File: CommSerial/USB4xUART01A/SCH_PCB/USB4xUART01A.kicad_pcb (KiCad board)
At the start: 2 copper layers, 40.1 x 40.1 mm, 31 parts, among them J1 HEADER_2x04_PARALLEL, J2 HEADER_2x04_PARALLEL, J3 HEADER_1x02, J4 HEADER_1x02, J5 HEADER_1x02, J6 HEADER_1x02, J7 HEADER_2x04_PARALLEL, J8 HEADER_2x04_PARALLEL, M1 HOLE, M2 HOLE, M3 HOLE, M4 HOLE

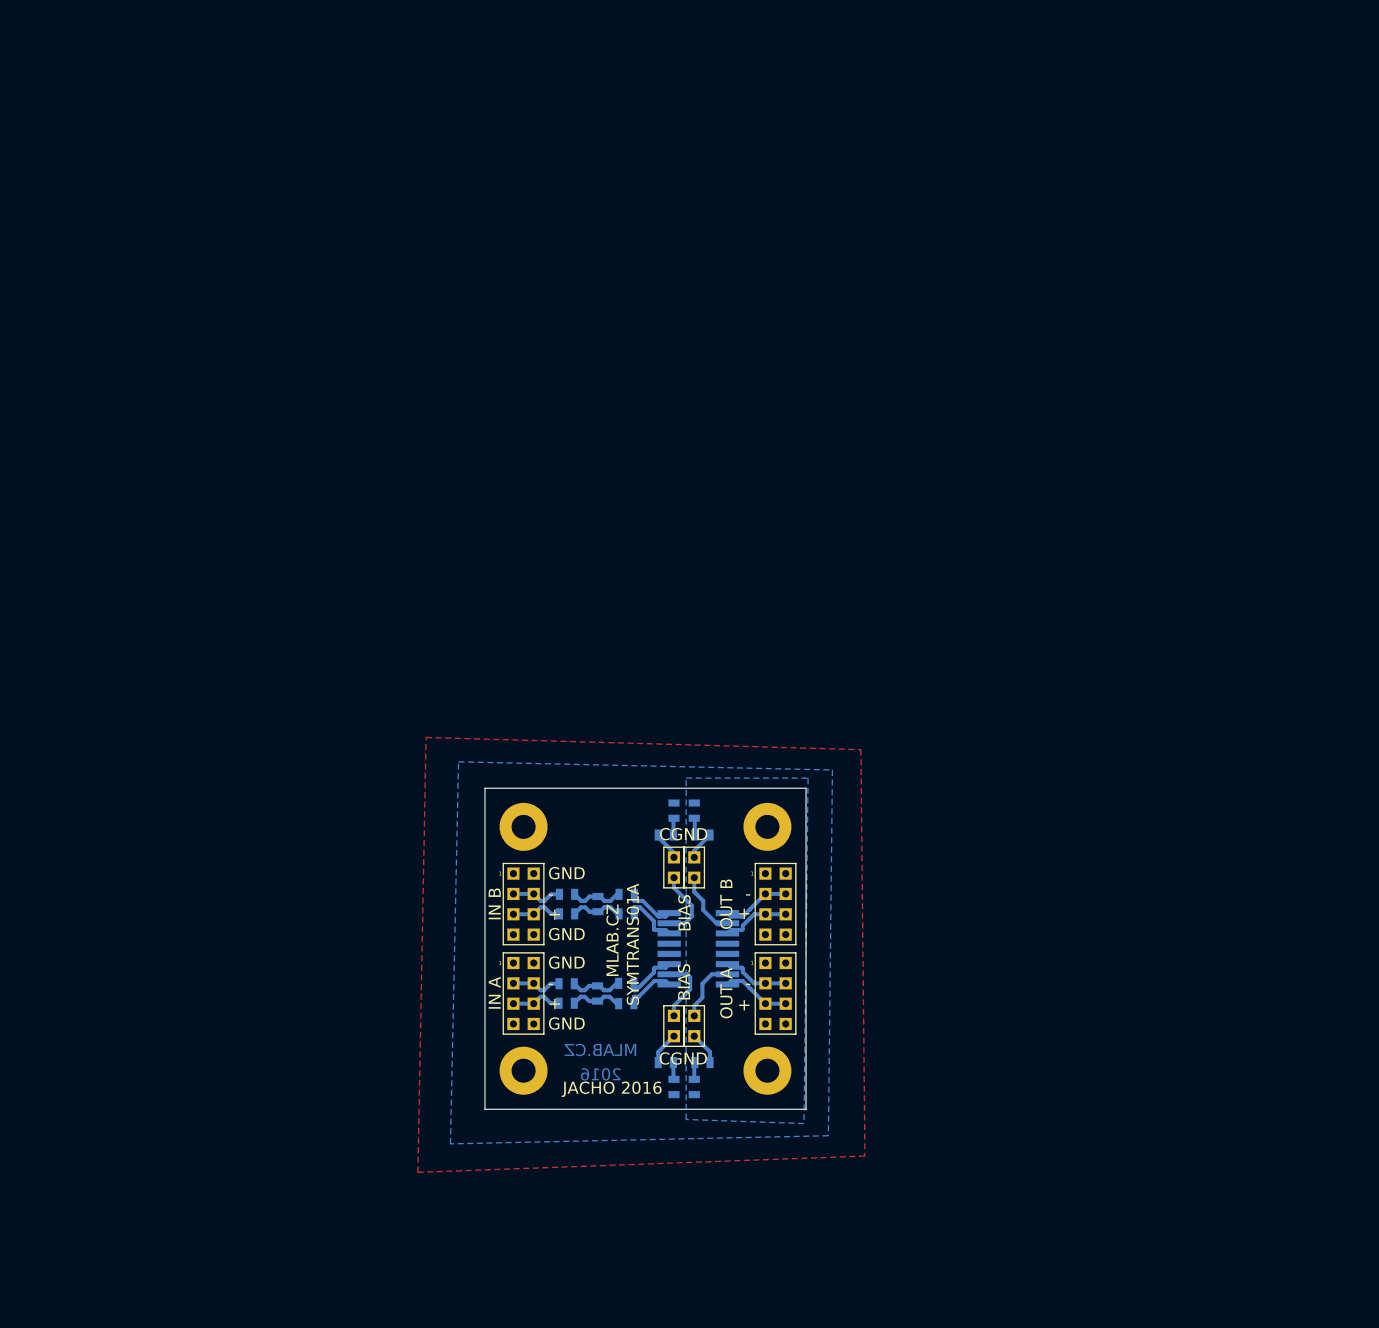
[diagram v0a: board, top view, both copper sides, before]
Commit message: 
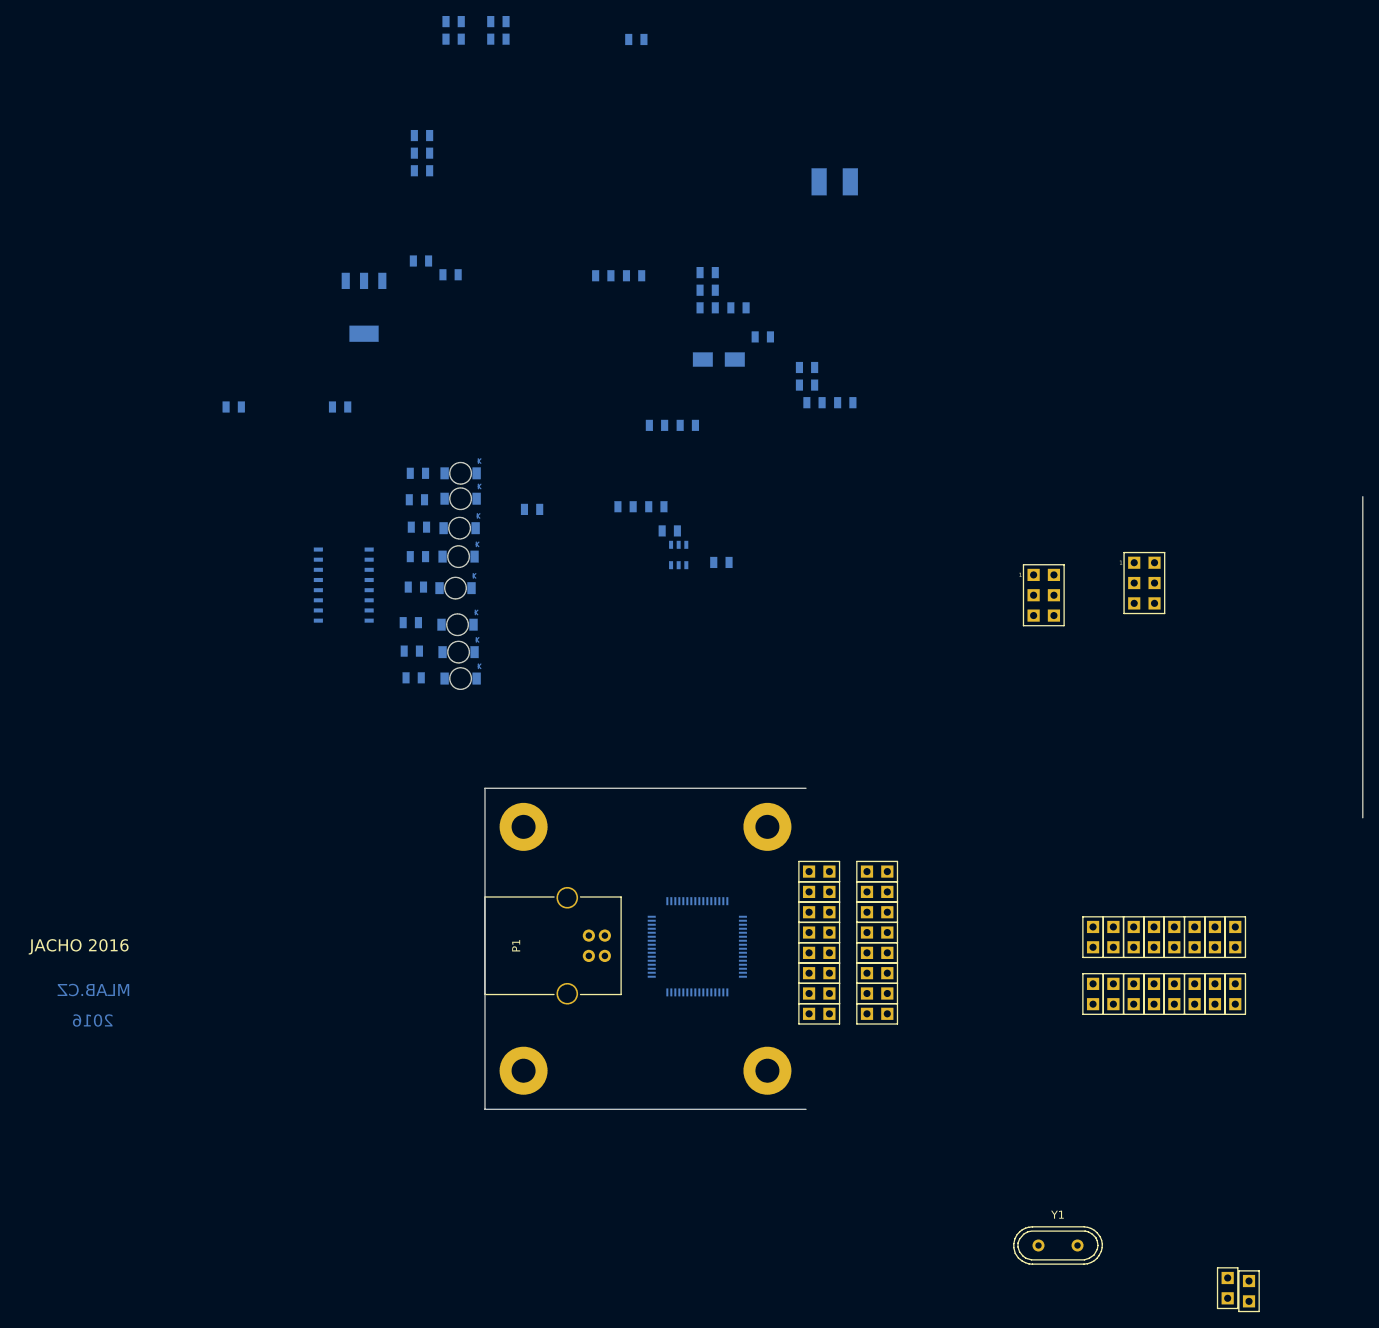
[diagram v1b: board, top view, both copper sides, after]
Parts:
- removed TR1: H1102NL, Mlab_TR:H110X_H1121_HX1188
- added C10: 100nF, Mlab_R:SMD-0805, B.Cu at (31.9, -100.4)
- added C11: 10uF, Mlab_R:SMD-0805, B.Cu at (6.14, -75.2)
- added C12: 100nF, Mlab_R:SMD-0805, B.Cu at (28.1, -104.8)
- added C13: 100nF, Mlab_R:SMD-0805, B.Cu at (25.6, -85.7)
- added C14: 10uF, Mlab_R:SMD-0805, B.Cu at (17.8, -75.6)
- added C15: 100nF, Mlab_R:SMD-0805, B.Cu at (28.1, -100.4)
- added C16: 100nF, Mlab_R:SMD-0805, B.Cu at (-4.05, -104.6)
- added C17: 100nF, Mlab_R:SMD-0805, B.Cu at (41.4, -88.6)
- added C18: 100nF, Mlab_R:SMD-0805, B.Cu at (21.7, -75.6)
- added C19: 100nF, Mlab_R:SMD-0805, B.Cu at (40.5, -93.0)
- added C20: 100nF, Mlab_R:SMD-0805, B.Cu at (18.9, -104.5)
- added C5: 27pF, Mlab_R:SMD-0805, B.Cu at (35.0, -96.8)
- added C6: 100nF, Mlab_R:SMD-0805, B.Cu at (23.4, -72.6)
- added C7: 10uF, Mlab_R:SMD-0805, B.Cu at (21.8, -85.7)
- added C8: 100nF, Mlab_R:SMD-0805, B.Cu at (15.0, -104.5)
- added C9: 10nF, Mlab_R:SMD-0805, B.Cu at (28.1, -102.6)
- added D1: M4, Mlab_D:Diode-SMA_Standard, B.Cu at (29.5, -94.0)
- added D2: RED, Mlab_D:LED_1206, B.Cu at (-2.79, -79.8)
- added D3: RED, Mlab_D:LED_1206, B.Cu at (-2.79, -76.6)
- added D4: RED, Mlab_D:LED_1206, B.Cu at (-2.92, -72.9)
- added D5: RED, Mlab_D:LED_1206, B.Cu at (-3.05, -69.3)
- added D6: RED, Mlab_D:LED_1206, B.Cu at (-3.43, -65.4)
- added D7: RED, Mlab_D:LED_1206, B.Cu at (-3.17, -60.8)
- added D8: RED, Mlab_D:LED_1206, B.Cu at (-3.05, -57.4)
- added D9: RED, Mlab_D:LED_1206, B.Cu at (-2.79, -54.1)
- added F1: 750mA, Mlab_F:1812, B.Cu at (44.0, -116.2)
- added J10: JUMP_2x1, Mlab_Pin_Headers:Straight_1x02, F.Cu at (49.3, -30.0)
- added J11: JUMP_2x1, Mlab_Pin_Headers:Straight_1x02, F.Cu at (49.3, -27.4)
- added J12: JUMP_2x1, Mlab_Pin_Headers:Straight_1x02, F.Cu at (49.3, -24.9)
- added J13: JUMP_2x1, Mlab_Pin_Headers:Straight_1x02, F.Cu at (49.3, -22.4)
- added J14: JUMP_2x1, Mlab_Pin_Headers:Straight_1x02, F.Cu at (49.3, -19.8)
- added J15: JUMP_2x1, Mlab_Pin_Headers:Straight_1x02, F.Cu at (49.3, -17.3)
- added J16: JUMP_2x1, Mlab_Pin_Headers:Straight_1x02, F.Cu at (49.3, -14.7)
- added J17: JUMP_2x1, Mlab_Pin_Headers:Straight_1x02, F.Cu at (49.3, -12.2)
- added J18: JUMP_2x1, Mlab_Pin_Headers:Straight_1x02, F.Cu at (94.0, -21.8)
- added J19: JUMP_2x1, Mlab_Pin_Headers:Straight_1x02, F.Cu at (91.5, -21.8)
- added J20: JUMP_2x1, Mlab_Pin_Headers:Straight_1x02, F.Cu at (89.0, -21.8)
- added J21: JUMP_2x1, Mlab_Pin_Headers:Straight_1x02, F.Cu at (86.4, -21.8)
- added J22: JUMP_2x1, Mlab_Pin_Headers:Straight_1x02, F.Cu at (83.9, -21.8)
- added J23: JUMP_2x1, Mlab_Pin_Headers:Straight_1x02, F.Cu at (81.3, -21.8)
- added J24: JUMP_2x1, Mlab_Pin_Headers:Straight_1x02, F.Cu at (78.8, -21.8)
- added J25: JUMP_2x1, Mlab_Pin_Headers:Straight_1x02, F.Cu at (76.3, -21.8)
- added J26: JUMP_2x1, Mlab_Pin_Headers:Straight_1x02, F.Cu at (94.0, -14.7)
- added J27: JUMP_2x1, Mlab_Pin_Headers:Straight_1x02, F.Cu at (91.5, -14.7)
- added J28: JUMP_2x1, Mlab_Pin_Headers:Straight_1x02, F.Cu at (89.0, -14.7)
- added J29: JUMP_2x1, Mlab_Pin_Headers:Straight_1x02, F.Cu at (86.4, -14.7)
- added J30: JUMP_2x1, Mlab_Pin_Headers:Straight_1x02, F.Cu at (83.9, -14.7)
- added J31: JUMP_2x1, Mlab_Pin_Headers:Straight_1x02, F.Cu at (81.3, -14.7)
- added J32: JUMP_2x1, Mlab_Pin_Headers:Straight_1x02, F.Cu at (78.8, -14.7)
- added J33: JUMP_2x1, Mlab_Pin_Headers:Straight_1x02, F.Cu at (76.3, -14.7)
- added J34: JUMP_2x1, Mlab_Pin_Headers:Straight_1x02, F.Cu at (93.1, 22.1)
- added J35: JUMP_3X2, Mlab_Pin_Headers:Straight_2x03, F.Cu at (70.1, -64.5)
- added J36: JUMP_3X2, Mlab_Pin_Headers:Straight_2x03, F.Cu at (82.7, -66.0)
- added J9: JUMP_2x1, Mlab_Pin_Headers:Straight_1x02, F.Cu at (42.0, -12.2)
- added L1: BLM21PG300SN1, Mlab_R:SMD-0805, B.Cu at (-3.67, -136.2)
- added L2: BLM21PG300SN1, Mlab_R:SMD-0805, B.Cu at (-3.67, -134.0)
- added L3: BLM21PG300SN1, Mlab_R:SMD-0805, B.Cu at (-31.2, -88.0)
- added P1: USB_B, Connect:USB_B, F.Cu at (15.2, -19.4)
- added R15: 10k, Mlab_R:SMD-0805, B.Cu at (-7.75, -106.3)
- added U1: 93LC56BT-I/OT, Mlab_IO:SOT-23-6, B.Cu at (24.5, -69.5)
- added U2: FT4232HL, Housings_QFP:LQFP-64_10x10mm_Pitch0.5mm, B.Cu at (26.8, -20.6)
- added U3: LM1117_3V3, Mlab_IO:SOT-223, B.Cu at (-14.9, -100.5)
- added U4: SN74HC595D, SMD_Packages:SO-16-N, B.Cu at (-17.4, -65.8)
- added Y1: 12MHz, Mlab_XTAL:Crystal_HC49-U_Vertical, F.Cu at (71.9, 16.8)
- C2, C4: value 100nF -> 10uF
- C3: value 100nF -> 27pF
- J1, J2, J7, J8: value HEADER_2x04_PARALLEL -> JUMP_2x1; footprint Mlab_Pin_Headers:Straight_2x04 -> Mlab_Pin_Headers:Straight_1x02
- J3, J4, J5, J6: value HEADER_1x02 -> JUMP_2x1; footprint Mlab_Pin_Headers:Straight_2x01 -> Mlab_Pin_Headers:Straight_1x02
- R1, R3, R4: value 300 -> 10k
- R10, R9: value - -> 300R
- R11, R12, R13, R14, R7, R8: value 0 -> 300R
- R2: value 300 -> 2k
- R5: value 0 -> 1k
- R6: value 0 -> 12k
- moved R3 121.1 mm to (-7.62, -122.0), turned to 0 degrees
- moved R1 117.7 mm to (-7.62, -119.8)
- moved R5 111.9 mm to (1.93, -136.2), turned to 0 degrees
- moved R6 107.2 mm to (19.2, -134.0), turned to 0 degrees
- moved R4 102.7 mm to (1.93, -134.0), turned to 0 degrees
- moved J1 98.0 mm to (95.8, 22.5)
- moved C1 94.7 mm to (-17.9, -88.0), turned to 0 degrees
- moved R2 88.4 mm to (-7.62, -117.6)
- moved C3 87.6 mm to (45.3, -88.6), turned to 0 degrees
- moved R7 68.8 mm to (-8.13, -79.8), turned to 0 degrees
- moved R8 63.3 mm to (-8.26, -76.5), turned to 0 degrees
- moved R10 59.0 mm to (-8.13, -69.3), turned to 0 degrees
- moved C2 55.7 mm to (40.5, -90.8), turned to 0 degrees
- moved R9 52.2 mm to (-8.00, -73.0), turned to 0 degrees
- moved R13 51.6 mm to (-8.89, -57.5), turned to 0 degrees
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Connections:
- C1 pad 1: Net-(C1-Pad1) -> +3V3
- C3 pad 2: GNDA -> GND
- C4 pad 2: GNDA -> GND
- J1 pad 1: GND -> /RES
- J1 pad 2: GND -> /RES
- J2 pad 1: GND -> /A_TXD
- J2 pad 2: GND -> /A_TXD
- J3 pad 1: Net-(J3-Pad1) -> /A_RXD
- J3 pad 2: Net-(J3-Pad2) -> /A_RXD
- J4 pad 1: Net-(J4-Pad1) -> /A_RTS
- J4 pad 2: Net-(J4-Pad2) -> /A_RTS
- J5 pad 1: Net-(J5-Pad1) -> /A_CTS
- J5 pad 2: Net-(J5-Pad2) -> /A_CTS
- J6 pad 1: Net-(J6-Pad1) -> /A_DTR
- J6 pad 2: Net-(J6-Pad2) -> /A_DTR
- J7 pad 1: GNDA -> /A_DSR
- J7 pad 2: GNDA -> /A_DSR
- J8 pad 1: GNDA -> /A_DCD
- J8 pad 2: GNDA -> /A_DCD
- R1 pad 1: Net-(J3-Pad2) -> Net-(R1-Pad1)
- R1 pad 2: Net-(C1-Pad1) -> +3V3
- R10 pad 1: /A2+ -> /D
- R10 pad 2: /A2- -> Net-(D5-Pad2)
- R11 pad 1: /B3+ -> /E
- R11 pad 2: /B2+ -> Net-(D6-Pad2)
- R12 pad 1: /B3- -> /F
- R12 pad 2: /B2- -> Net-(D7-Pad2)
- R13 pad 1: /A3+ -> /G
- R13 pad 2: /A2+ -> Net-(D8-Pad2)
- R14 pad 1: /A3- -> /H
- R14 pad 2: /A2- -> Net-(D9-Pad2)
- R2 pad 1: Net-(J4-Pad2) -> /EEDATA
- R2 pad 2: Net-(C2-Pad1) -> Net-(R1-Pad1)
- R3 pad 1: Net-(J5-Pad2) -> /EECLK
- R3 pad 2: Net-(C3-Pad1) -> +3V3
- R4 pad 1: Net-(J6-Pad2) -> /EECS
- R4 pad 2: Net-(C4-Pad1) -> +3V3
- R5 pad 1: /B2+ -> /RES
- R5 pad 2: /BIN+ -> +3V3
- R6 pad 1: /B2- -> Net-(R6-Pad1)
- R6 pad 2: /BIN- -> GND
- R7 pad 1: /A2+ -> /A
- R7 pad 2: /AIN+ -> Net-(D2-Pad2)
- R8 pad 1: /A2- -> /B
- R8 pad 2: /AIN- -> Net-(D3-Pad2)
- R9 pad 1: /B2+ -> /C
- R9 pad 2: /B2- -> Net-(D4-Pad2)
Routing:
- net Net-(J4-Pad1): track 8.95 -> 0.00 mm
- net /BOUT-: track 8.64 -> 0.00 mm
- net /AOUT+: track 8.64 -> 0.00 mm
- net /BOUT+: track 8.54 -> 0.00 mm
- net /AOUT-: track 8.54 -> 0.00 mm
- net Net-(J3-Pad1): track 8.44 -> 0.00 mm
- net Net-(J6-Pad1): track 8.23 -> 0.00 mm
- net Net-(J5-Pad1): track 8.06 -> 0.00 mm
- net /B3+: track 7.13 -> 0.00 mm
- net /A2+: track 6.96 -> 0.00 mm
- net /A2-: track 6.96 -> 0.00 mm
- net /B2-: track 6.94 -> 0.00 mm
- net /B2+: track 6.94 -> 0.00 mm
- net /A3-: track 6.93 -> 0.00 mm
- net /BIN-: track 6.45 -> 0.00 mm
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- removed copper zone on B.Cu, net GND
- removed copper zone on F.Cu, net GND
- removed copper zone on B.Cu, net GNDA
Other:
- board size 40.1 x 40.1 mm -> 109.7 x 76.6 mm
- board text removed: "+"
- board text removed: "-"
- board text removed: "BIAS"
- board text removed: "CGND"
- board text removed: "GND"
- board text removed: "IN A"
- board text removed: "IN B"
- board text removed: "OUT A"
- board text removed: "OUT B"
- board text removed: "SYMTRANS01A"

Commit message: 
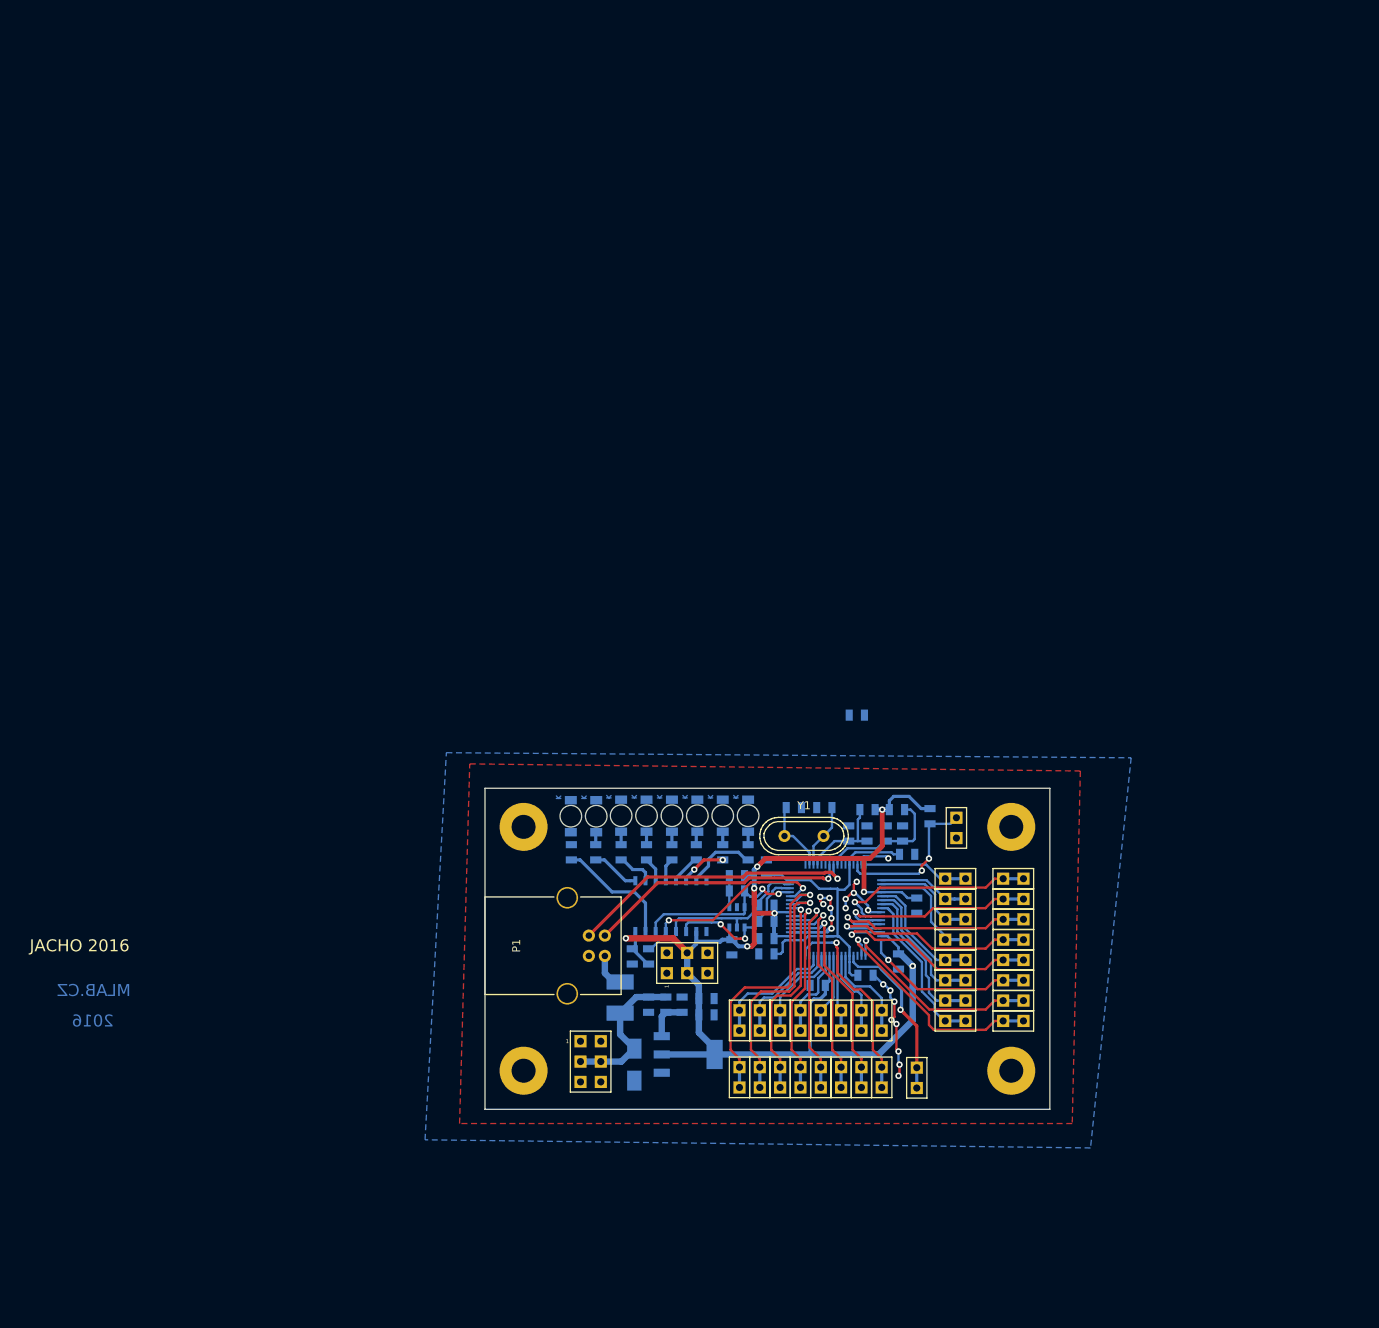
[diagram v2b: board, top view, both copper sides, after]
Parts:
- removed C17: 100nF, Mlab_R:SMD-0805
- added C21: 100nF, Mlab_R:SMD-0805, B.Cu at (35.4, -21.6)
- moved R4 113.3 mm to (35.4, -25.8)
- moved R5 113.0 mm to (55.9, -36.9), turned to 90 degrees
- moved L1 113.0 mm to (51.8, -37.7)
- moved L2 109.3 mm to (48.1, -37.7), turned to 180 degrees
- moved R3 107.2 mm to (35.4, -23.7)
- moved F1 105.4 mm to (17.1, -14.2), turned to 270 degrees
- moved U3 101.8 mm to (25.7, -7.11), turned to 90 degrees
- moved R1 98.5 mm to (31.8, -29.5)
- moved R2 98.2 mm to (31.8, -27.6), turned to 180 degrees
- moved C16 92.2 mm to (53.0, -32.1)
- moved L3 92.2 mm to (22.9, -13.3), turned to 270 degrees
- moved R15 91.5 mm to (20.7, -19.4), turned to 270 degrees
- moved C12 90.2 mm to (41.8, -15.7), turned to 180 degrees
- moved C9 89.6 mm to (20.7, -13.3), turned to 270 degrees
- moved R6 88.8 mm to (46.7, -49.5)
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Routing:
- net +3V3: track 0.00 -> 185.3 mm, vias 0 -> 8
- net +1V8: track 0.00 -> 44.5 mm
- net GND: track 0.00 -> 44.5 mm, vias 0 -> 20
- net Net-(P1-Pad3): track 0.00 -> 36.7 mm, vias 0 -> 1
- net /D_RI: track 0.00 -> 35.3 mm, vias 0 -> 1
- net Net-(P1-Pad2): track 0.00 -> 32.8 mm, vias 0 -> 1
- net /D_DCD: track 0.00 -> 32.2 mm, vias 0 -> 1
- net /B_RI: track 0.00 -> 29.0 mm, vias 0 -> 1
- net /B_CTS: track 0.00 -> 28.0 mm, vias 0 -> 1
- net /B_DTR: track 0.00 -> 27.8 mm, vias 0 -> 1
- net /D_RTS: track 0.00 -> 27.6 mm, vias 0 -> 1
- net /B_RTS: track 0.00 -> 27.5 mm, vias 0 -> 1
- net /D_CTS: track 0.00 -> 27.2 mm, vias 0 -> 1
- net /D_RXD: track 0.00 -> 27.0 mm, vias 0 -> 1
- net /D_DSR: track 0.00 -> 26.6 mm, vias 0 -> 1
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- added copper zone on B.Cu, net GND
- added copper zone on F.Cu, net GND
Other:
- board size 109.7 x 76.6 mm -> 70.6 x 40.1 mm
